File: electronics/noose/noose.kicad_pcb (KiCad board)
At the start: 2 copper layers, 8 parts, among them J1 JACK, P1 IN_CABLE, P2 NOOSE_CABLE

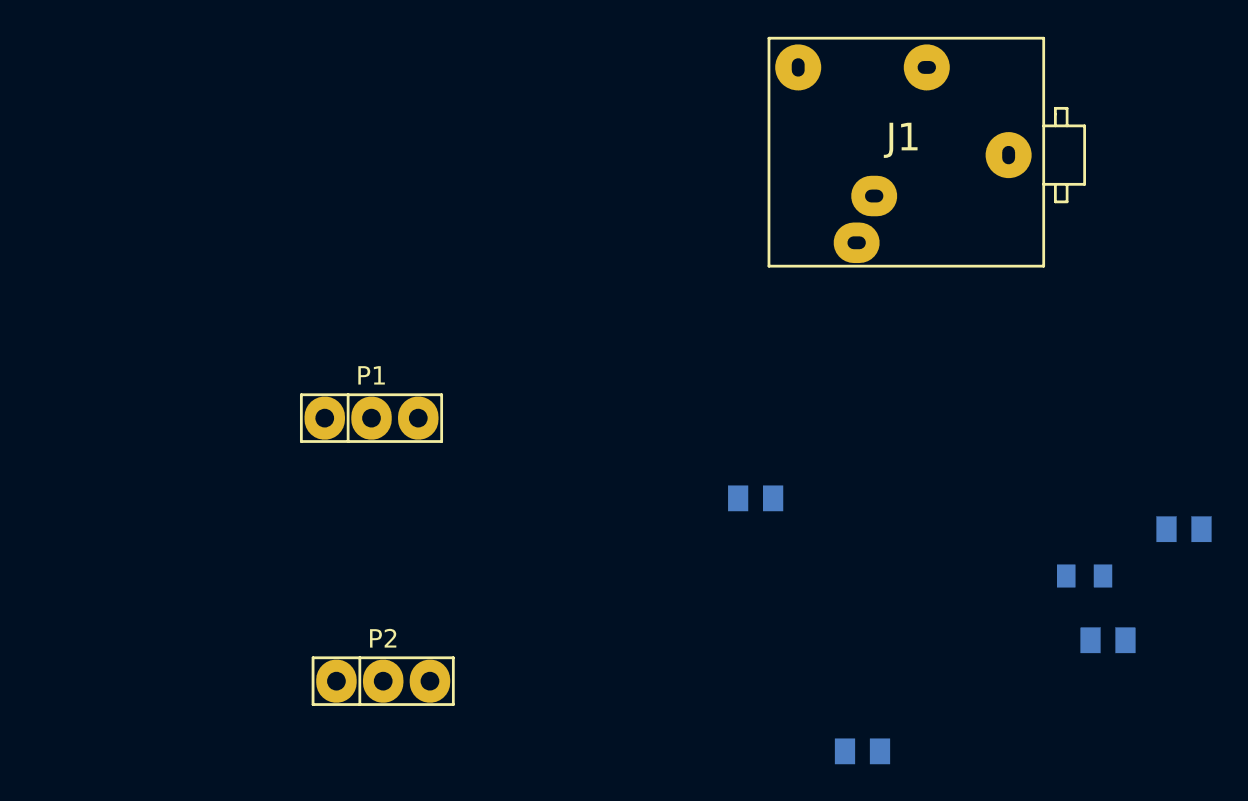
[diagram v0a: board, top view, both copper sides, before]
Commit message: draw pcb for noose
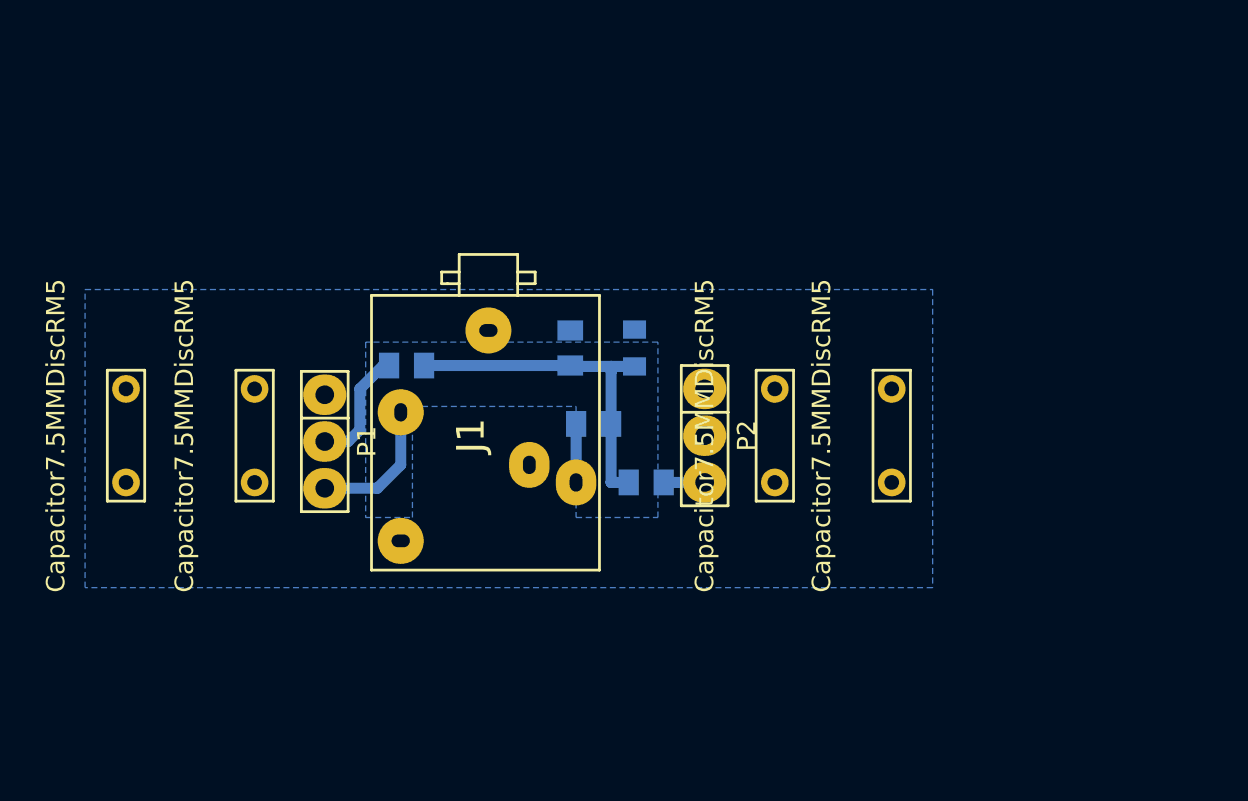
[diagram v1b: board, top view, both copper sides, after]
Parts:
- added Capacitor7.5MMDiscRM5: VAL**, Capacitors_ThroughHole:Capacitor7.5MMDiscRM5, F.Cu at (114.3, 101.6)
- added Capacitor7.5MMDiscRM5: VAL**, Capacitors_ThroughHole:Capacitor7.5MMDiscRM5, F.Cu at (121.3, 101.6)
- added Capacitor7.5MMDiscRM5: VAL**, Capacitors_ThroughHole:Capacitor7.5MMDiscRM5, F.Cu at (155.9, 101.6)
- added Capacitor7.5MMDiscRM5: VAL**, Capacitors_ThroughHole:Capacitor7.5MMDiscRM5, F.Cu at (149.5, 101.6)
- moved R2 43.2 mm to (129.5, 97.8), turned to 180 degrees
- moved R4 33.2 mm to (138.4, 96.8), turned to 270 degrees
- moved C1 27.4 mm to (141.9, 96.8), turned to 90 degrees
- moved J1 27.2 mm to (134.0, 101.6), turned to 90 degrees
- moved R1 23.0 mm to (139.7, 101.0)
- moved P2 22.0 mm to (145.7, 101.6), turned to 270 degrees
- moved R3 6.01 mm to (142.6, 104.1), turned to 180 degrees
- moved P1 2.84 mm to (125.1, 101.9), turned to 270 degrees
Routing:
- net Net-(C1-Pad1): track 0.00 -> 18.6 mm
- net Net-(J1-Pad3): track 0.00 -> 7.51 mm
- net Net-(P1-Pad2): track 0.00 -> 6.51 mm
- net Net-(J1-Pad4): track 0.00 -> 3.18 mm
- net Net-(P2-Pad3): track 0.00 -> 2.22 mm
- added copper zone on B.Cu, net GND

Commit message: plot boards
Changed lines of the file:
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@@
 (kicad_pcb (version 4) (host pcbnew "(2015-11-08 BZR 6303, Git 5897580)-product")
   (general
-    (links 0)
+    (links 21)
     (no_connects 0)
-    (area 0 0 0 0)
+    (area 109.555 91.672499 158.115001 110.708809)
     (thickness 1.6)
     (drawings 0)
@@
     (mod_text_size 1 1)
     (mod_text_width 0.15)
-    (pad_size 1.50114 1.50114)
-    (pad_drill 0.8001)
+    (pad_size 2.5 2.5)
+    (pad_drill 0.7)
     (pad_to_mask_clearance 0.2)
     (aux_axis_origin 0 0)
     (visible_elements FFFFF71F)
     (pcbplotparams
-      (layerselection 0x00030_80000001)
+      (layerselection 0x00000_80000000)
       (usegerberextensions false)
       (excludeedgelayer true)
@@
       (padsonsilk false)
       (subtractmaskfromsilk false)
-      (outputformat 1)
+      (outputformat 5)
       (mirror false)
       (drillshape 1)
@@
     (fp_line (start 7.62 -6.35) (end -7.3025 -6.35) (layer F.SilkS) (width 0.15))
     (fp_line (start -7.3025 -6.35) (end -7.3025 6.0325) (layer F.SilkS) (width 0.15))
-    (pad 2 thru_hole circle (at -5.715 -4.7625 90) (size 2.5 2.5) (drill oval 0.7 1) (layers *.Cu *.Mask F.SilkS))
-    (pad 1 thru_hole circle (at 5.715 0 90) (size 2.5 2.5) (drill oval 0.7 1) (layers *.Cu *.Mask F.SilkS)
+    (pad 2 thru_hole circle (at -5.715 -4.7625 90) (size 2.5 2.5) (drill 0.7) (layers *.Cu *.Mask F.SilkS))
+    (pad 1 thru_hole circle (at 5.715 0 90) (size 2.5 2.5) (drill 0.7) (layers *.Cu *.Mask F.SilkS)
       (net 2 GND))
-    (pad 4 thru_hole oval (at -2.54 4.7625 90) (size 2.5 2.2) (drill oval 1 0.7) (layers *.Cu *.Mask F.SilkS)
+    (pad 4 thru_hole circle (at -2.54 4.7625 90) (size 2.5 2.5) (drill 0.7) (layers *.Cu *.Mask F.SilkS)
       (net 3 "Net-(J1-Pad4)"))
-    (pad 5 thru_hole oval (at -1.5875 2.2225 90) (size 2.5 2.2) (drill oval 1 0.7) (layers *.Cu *.Mask F.SilkS))
-    (pad 3 thru_hole circle (at 1.27 -4.7625 90) (size 2.5 2.5) (drill oval 1 0.7) (layers *.Cu *.Mask F.SilkS)
+    (pad 5 thru_hole circle (at -1.5875 2.2225 90) (size 2.5 2.5) (drill 0.7) (layers *.Cu *.Mask F.SilkS))
+    (pad 3 thru_hole circle (at 1.27 -4.7625 90) (size 2.5 2.5) (drill 0.7) (layers *.Cu *.Mask F.SilkS)
       (net 4 "Net-(J1-Pad3)"))
   )
